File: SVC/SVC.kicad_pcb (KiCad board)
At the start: 2 copper layers, 140.2 x 112 mm, 164 parts, among them J1 L1, J10 Inductor, J11 629722000214, J12 AVR-ISP-6, J2 L2, J3 L3, J4 C12, J5 C23, J6 C31, J7 PE, J8 Inductor, J9 Inductor, M1 Fan_4pin, Q1 DN2470, Q2 DN2470, Q3 DN2470, Q4 MMBT3906, Q5 MMBT3906, Q6 MMBT3906, Q7 MSC750SMA170S, SW1 SW_Push, T1 760871543, U1 FODM217D, U10 FODM217D, U11 UCC287506, U12 SI8932D-IS4, U13 AP7381-33SA-7, U14 ATmega32U4-A, U15 AD8620, U2 FODM217D, U3 FODM217D, U4 VOT8121AM, U5 VOT8121AM, U6 VOT8121AM, U7 LMC555xM, U8 LMC555xM, U9 LMC555xM, X1 831019275

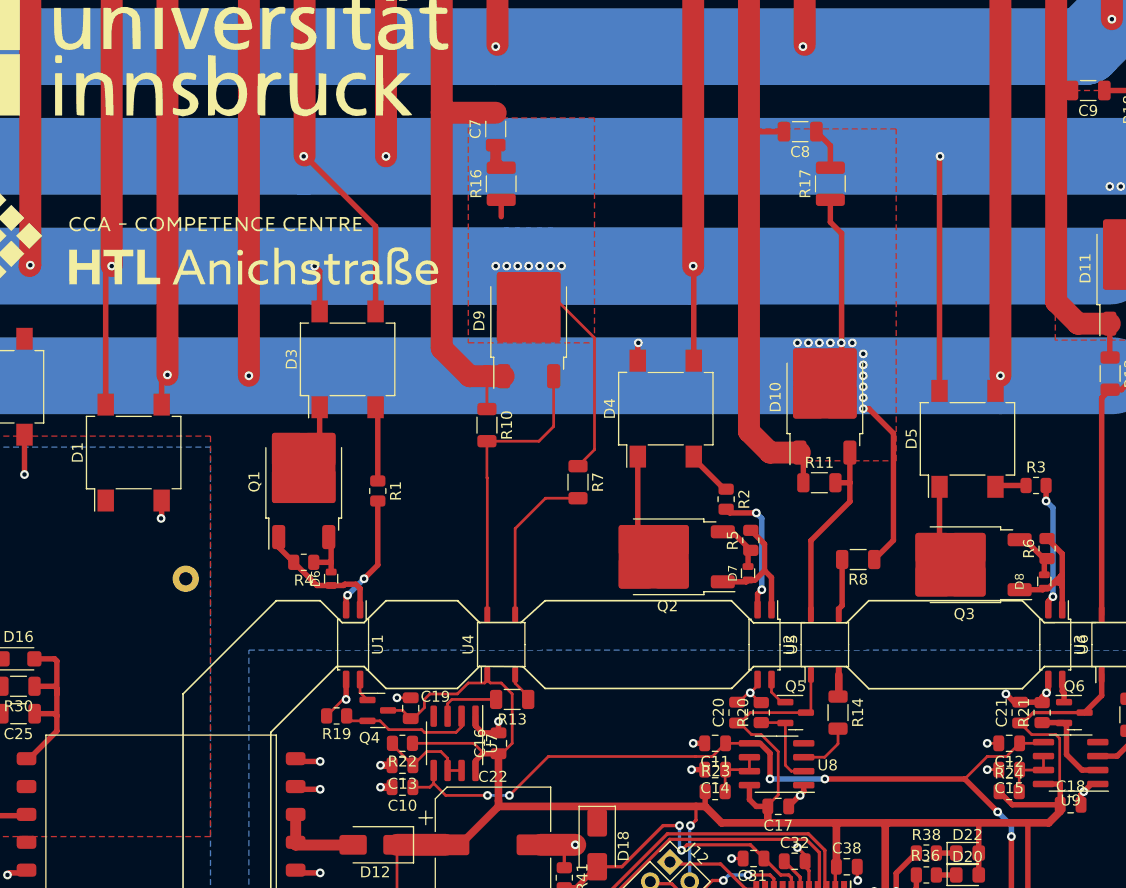
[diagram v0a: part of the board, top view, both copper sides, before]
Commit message: added some symbols, marked LV area as SELV
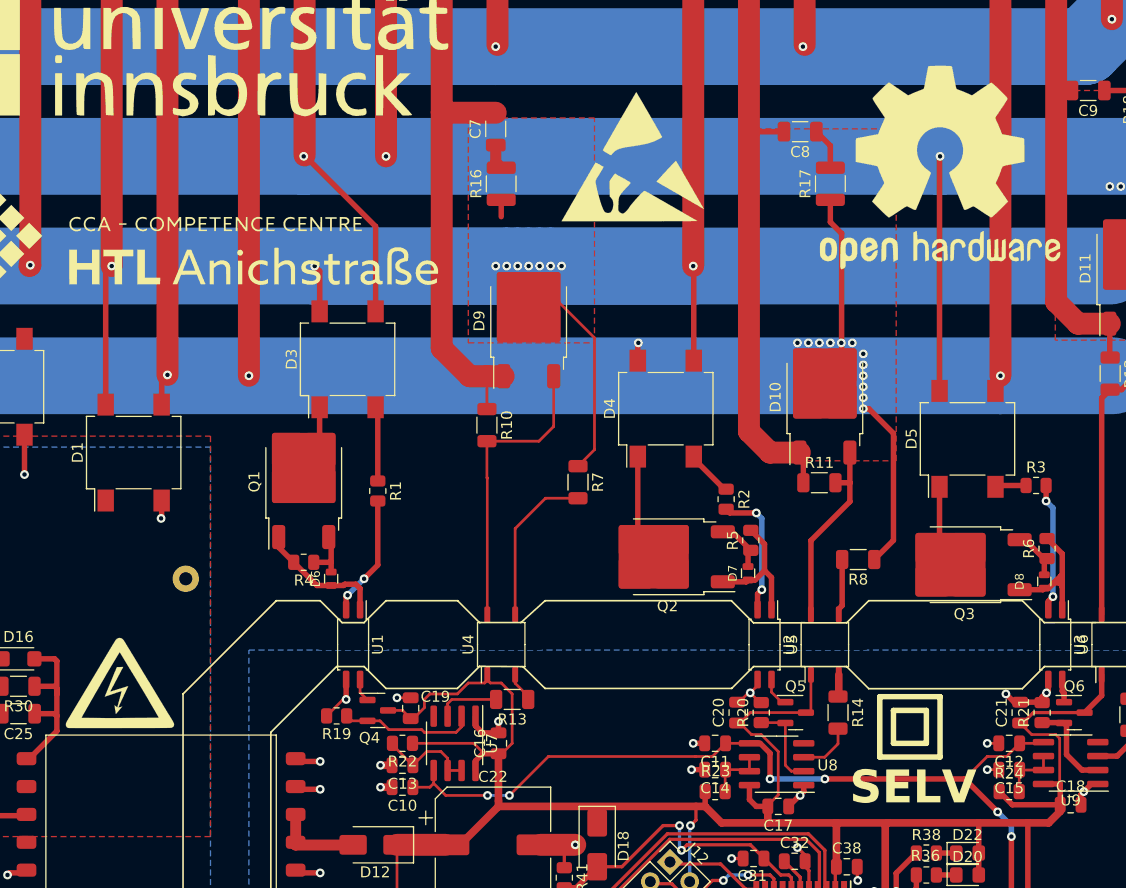
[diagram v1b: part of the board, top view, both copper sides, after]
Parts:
- added G***: LOGO, ctm:high_voltage_10x8, F.Cu at (95.8, 90.5)
- added REF**: OSHW-Logo2_24.3x20mm_SilkScreen, Symbol:OSHW-Logo2_24.3x20mm_SilkScreen, F.Cu at (170.5, 43.5)
- added REF**: ESD-Logo_13.2x12mm_SilkScreen, Symbol:ESD-Logo_13.2x12mm_SilkScreen, F.Cu at (142.5, 42.5)
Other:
- board text added: "SELV"
